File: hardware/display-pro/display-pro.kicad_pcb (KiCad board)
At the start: 2 copper layers, 57.8 x 58.4 mm, 19 parts, among them J2 POWER, J3 Input, J4 Output, J5 Clock, J6 Data, Q1 FQP30N06L, Q2 FQP30N06L

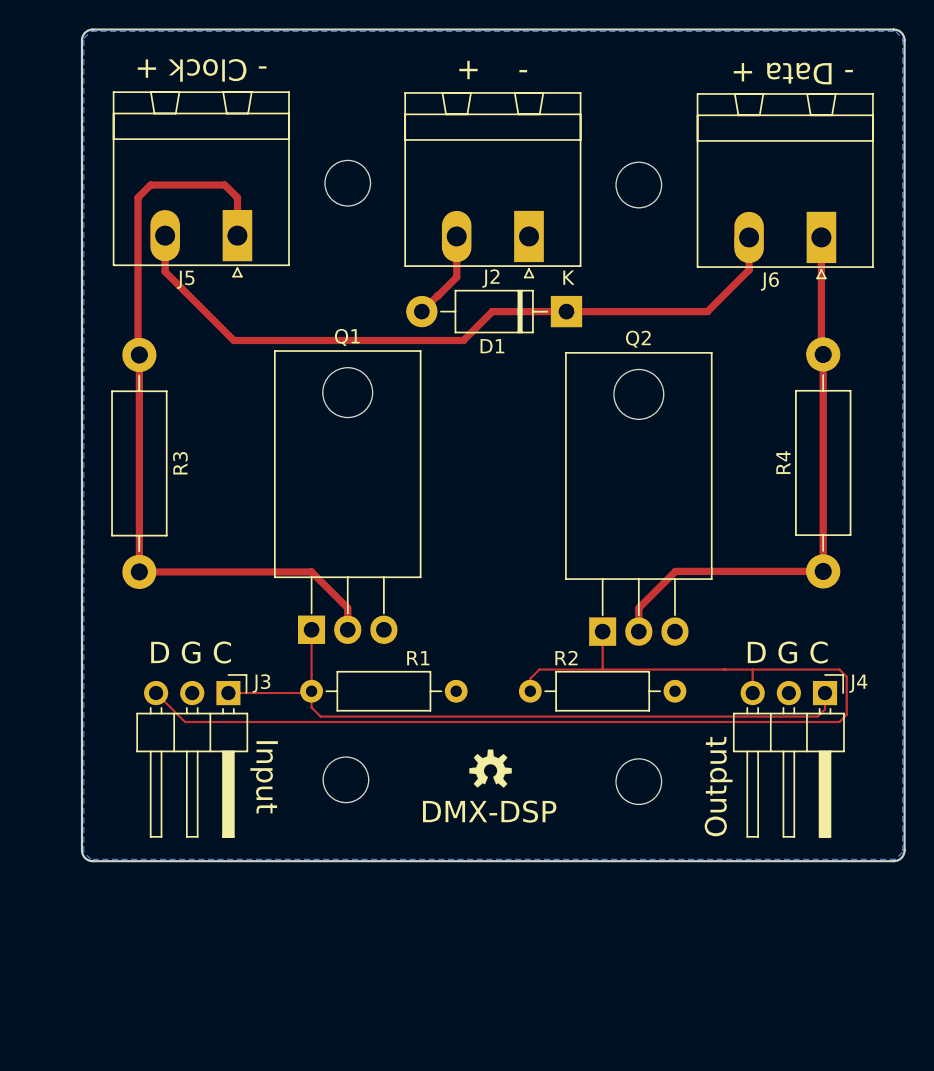
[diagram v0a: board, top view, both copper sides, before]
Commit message: Prototype version of DMX, Analog, and PWM IO Modules and both TX and RX IO interfaces.
Make io-analog a stackable family
io-analog-core handles D to A
io-analog-voltage handles voltage output
io-analog-pwm handles pwm output for leds, drive display pro

Refactor display-pro to work with io-analog-pwm
Add correct coax power connector

Move TX2 to tx-io
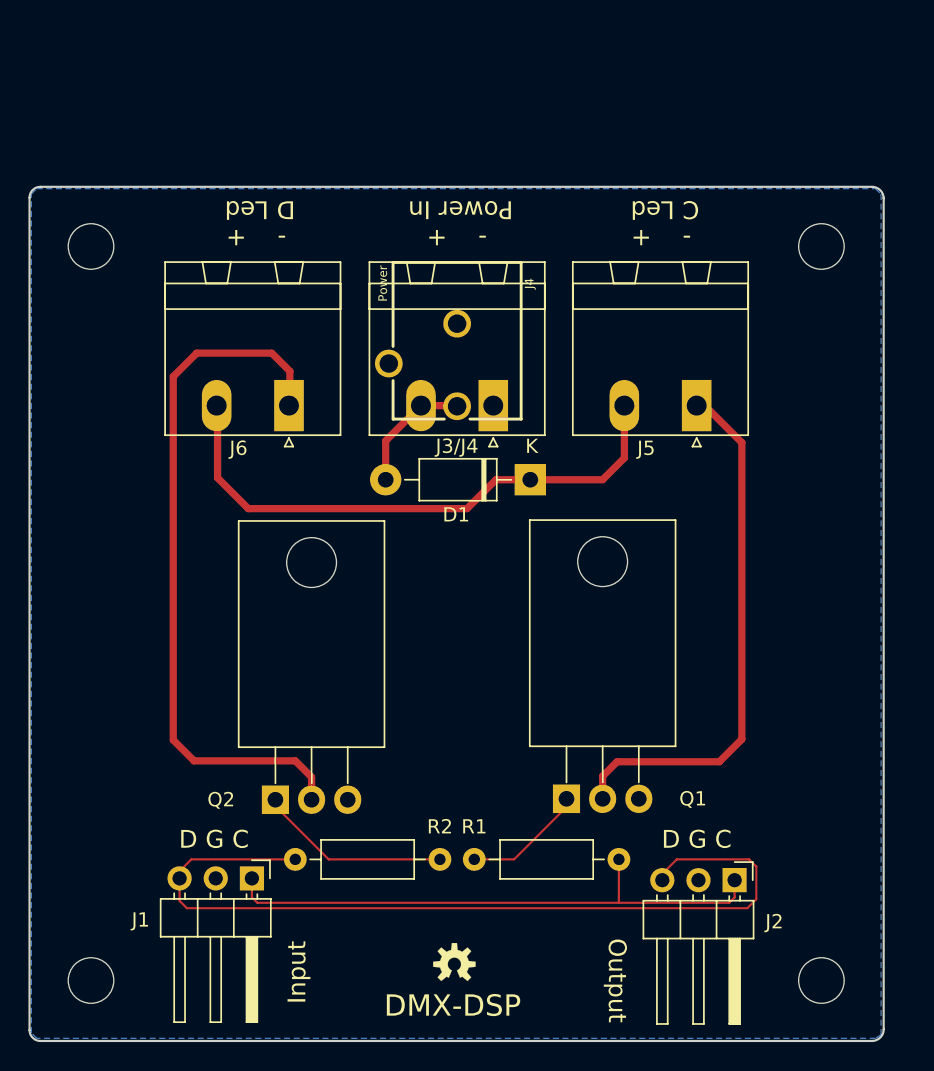
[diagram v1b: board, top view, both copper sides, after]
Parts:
- removed the ? at (146.9, 80.1)
- removed R3, R4: R?, Resistor_THT:R_Axial_DIN0411_L9.9mm_D3.6mm_P15.24mm_Horizontal
- added J1: Input, Connector_PinHeader_2.54mm:PinHeader_1x03_P2.54mm_Horizontal, F.Cu at (130.0, 109.2)
- J2: value POWER -> Output; footprint Connector_Phoenix_MSTB:PhoenixContact_MSTBA_2,5_2-G-5,08_1x02_P5.08mm_Horizontal -> Connector_PinHeader_2.54mm:PinHeader_1x03_P2.54mm_Horizontal
- J3: value Input -> Power; footprint Connector_PinHeader_2.54mm:PinHeader_1x03_P2.54mm_Horizontal -> Connector_Phoenix_MSTB:PhoenixContact_MSTBA_2,5_2-G-5,08_1x02_P5.08mm_Horizontal
- J4: value Output -> Power; footprint Connector_PinHeader_2.54mm:PinHeader_1x03_P2.54mm_Horizontal -> Connectors:POWER_JACK_PTH_BREAD
- J5: value Clock -> C Out
- J6: value Data -> D Out
- moved J2 47.5 mm to (164.0, 109.3), turned to 270 degrees
- moved J4 42.6 mm to (144.5, 62.3), turned to 180 degrees
- moved J6 39.2 mm to (132.7, 75.9)
- moved J5 34.4 mm to (161.3, 75.9)
- moved G*** 32.9 mm to (133.9, 116.6)
- moved J3 27.5 mm to (147.0, 75.9), turned to 180 degrees
- moved Q2 25.8 mm to (131.7, 103.6)
- moved MH3 22.8 mm to (118.7, 116.3)
- moved Q1 21.5 mm to (152.1, 103.6)
- moved R2 20.3 mm to (143.3, 107.8)
- moved MH4 19.0 mm to (170.1, 116.3)
- moved MH1 18.6 mm to (118.7, 64.8)
- moved ? 13.8 mm to (144.3, 115.2)
- moved MH2 13.5 mm to (170.1, 64.8)
- moved D1 12.1 mm to (149.6, 81.2)
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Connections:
- J2 pad 1: GND -> /C
- J2 pad 2: Net-(D1-Pad2) -> GND
- J3 pad 1: /CLOCK -> GND
- J3 pad 2: GND -> Net-(D1-Pad2)
- Q1 pad 1: /CLOCK -> Net-(Q1-Pad1)
- Q2 pad 1: /DATA -> Net-(Q2-Pad1)
- R1 pad 1: GND -> Net-(Q1-Pad1)
- R1 pad 2: /CLOCK -> /C
- R2 pad 1: GND -> Net-(Q2-Pad1)
- R2 pad 2: /DATA -> /D
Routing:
- net /DATA: track 80.3 -> 0.00 mm
- net /D: track 0.00 -> 61.5 mm
- net /CLOCK: track 49.0 -> 0.00 mm
- net /C: track 0.00 -> 39.8 mm
- net Net-(J5-Pad1): track 53.9 -> 37.5 mm
- net Net-(Q2-Pad1): track 0.00 -> 13.6 mm
- net +VDC: track 50.7 -> 39.7 mm
- net Net-(J6-Pad1): track 39.2 -> 49.7 mm
- net Net-(Q1-Pad1): track 0.00 -> 8.51 mm
- net Net-(D1-Pad2): track 6.31 -> 8.79 mm
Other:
- board size 57.8 x 58.4 mm -> 60 x 60 mm
- board text added: "- + C Led"
- board text added: "- + D Led"
- board text added: "- + Power In"
- board text added: "DMX-DSP, Rev 1.4 Crazy Giraffe Software"
- board text added: "J3/J4"
- board text removed: "+ -"
- board text removed: "- Clock +"
- board text removed: "- Data +"
- board text removed: "DMX-DSP, Rev 1.2 Crazy Giraffe Software"
